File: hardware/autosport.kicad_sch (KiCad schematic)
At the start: 11 parts

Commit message: Add the Cube project
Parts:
- removed J?: AS022-55SN, symbol Connector_Generic:Conn_2Rows-55Pins
- removed R26, R27, R28: 0R, symbol Device:R_Small
- added J2: AS022-55SN, Local_Library:AS022-55SN, symbol AS022-55SN:AS022-55SN
- added R21, R22, R23, R24: 0R, symbol Device:R_Small
- renumbered R21 to R25, R22 to R26, R23 to R27, R24 to R28, R25 to R29, R29 to R30, R30 to R31
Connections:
- net +24V: now also J2.1 (Pin_1), J2.2 (Pin_2), J2.29 (Pin_29)
- net 5V_AUX: now also J2.54 (Pin_54)
- net ANALOG_INPUT_IN1: now also R21.1
- net ANALOG_INPUT_IN2: now also R22.1
- net ANALOG_INPUT_IN3: now also R23.1
- net ANALOG_INPUT_IN4: now also R24.1
- net ASSI_OUT_B: now also J2.37 (Pin_37)
- net ASSI_OUT_G: now also J2.36 (Pin_36)
- net ASSI_OUT_R: now also J2.35 (Pin_35)
- net BRAKE_LIGHT_OUT: now also J2.30 (Pin_30)
- net CAN+: now also J2.3 (Pin_3)
- net CAN-: now also J2.4 (Pin_4)
- net CAN2+: now also J2.5 (Pin_5)
- net CAN2-: now also J2.6 (Pin_6)
- net FAN_OUT_L: now also J2.31 (Pin_31)
- net FAN_OUT_R: now also J2.32 (Pin_32)
- net GND: now also J2.27 (Pin_27), J2.28 (Pin_28), J2.55 (Pin_55)
- net MONO_TEMPERATURE_IN: now also J2.11 (Pin_11)
- net PUMP_OUT_L: now also J2.33 (Pin_33)
- net PUMP_OUT_R: now also J2.34 (Pin_34)
- net RTDS_OUT: now also J2.51 (Pin_51)
- net SAFETY_IN_ASMS: now also J2.44 (Pin_44)
- net SAFETY_IN_FW: now also J2.43 (Pin_43)
- net SAFETY_IN_HV: now also J2.42 (Pin_42)
- net SAFETY_IN_HVD: now also J2.40 (Pin_40)
- net SAFETY_IN_INV: now also J2.39 (Pin_39)
- net SAFETY_IN_RES: now also J2.41 (Pin_41)
- net SAFETY_IN_RFU1: now also J2.45 (Pin_45)
- net SAFETY_IN_RFU2: now also J2.46 (Pin_46)
- net WATER_PRESSURE_IN1: now also J2.7 (Pin_7)
- net WATER_PRESSURE_IN2: now also J2.8 (Pin_8)
- net WATER_TEMPERATURE_IN1: now also J2.9 (Pin_9)
- net WATER_TEMPERATURE_IN2: now also J2.10 (Pin_10)
- net at R26.2: now also J2.21 (Pin_21)
- net at R29.2: now also J2.24 (Pin_24)
- net at R27.2: now also J2.22 (Pin_22)
- net at R25.2: now also J2.20 (Pin_20)
- net at R28.2: now also J2.23 (Pin_23)
- net at R30.2: now also J2.25 (Pin_25)
- net at R31.2: now also J2.26 (Pin_26)
- new net: J2.14 (Pin_14), R21.2
- new net: J2.15 (Pin_15), R22.2
- new net: J2.16 (Pin_16), R23.2
- new net: J2.17 (Pin_17), R24.2
- new net ASSI_OUT_BUZZER: J2.38 (Pin_38)
- new net SAFETY_IN_WHEEL_FL: J2.47 (Pin_47)
- new net SAFETY_IN_WHEEL_FR: J2.48 (Pin_48)
- new net SAFETY_IN_WHEEL_RL: J2.49 (Pin_49)
- new net SAFETY_IN_WHEEL_RR: J2.50 (Pin_50)
- new net SUSPENSION_POT_IN_L: J2.12 (Pin_12)
- new net SUSPENSION_POT_IN_R: J2.13 (Pin_13)
- no-connect marks 3 -> 4
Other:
- note removed: "Additional interfaces"
- note removed: "RFU: Shielding?"
- moved on the sheet: R25, R26, R27, R28, R29, R30, R31

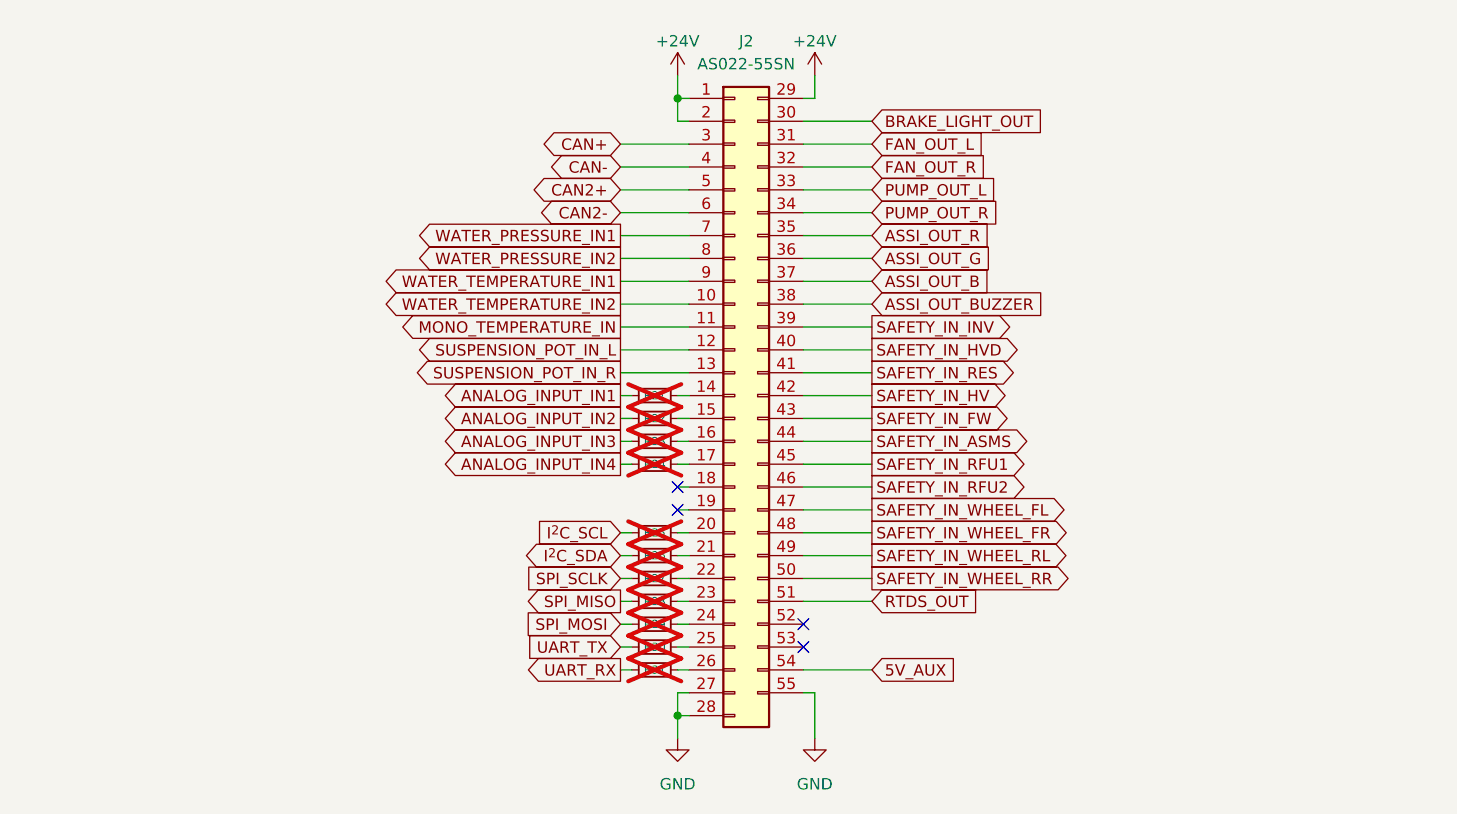
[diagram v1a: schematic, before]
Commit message: Improve the schematic
- add anti-aliasing filters
- rearrange the main connector signals
- improve the power filtering
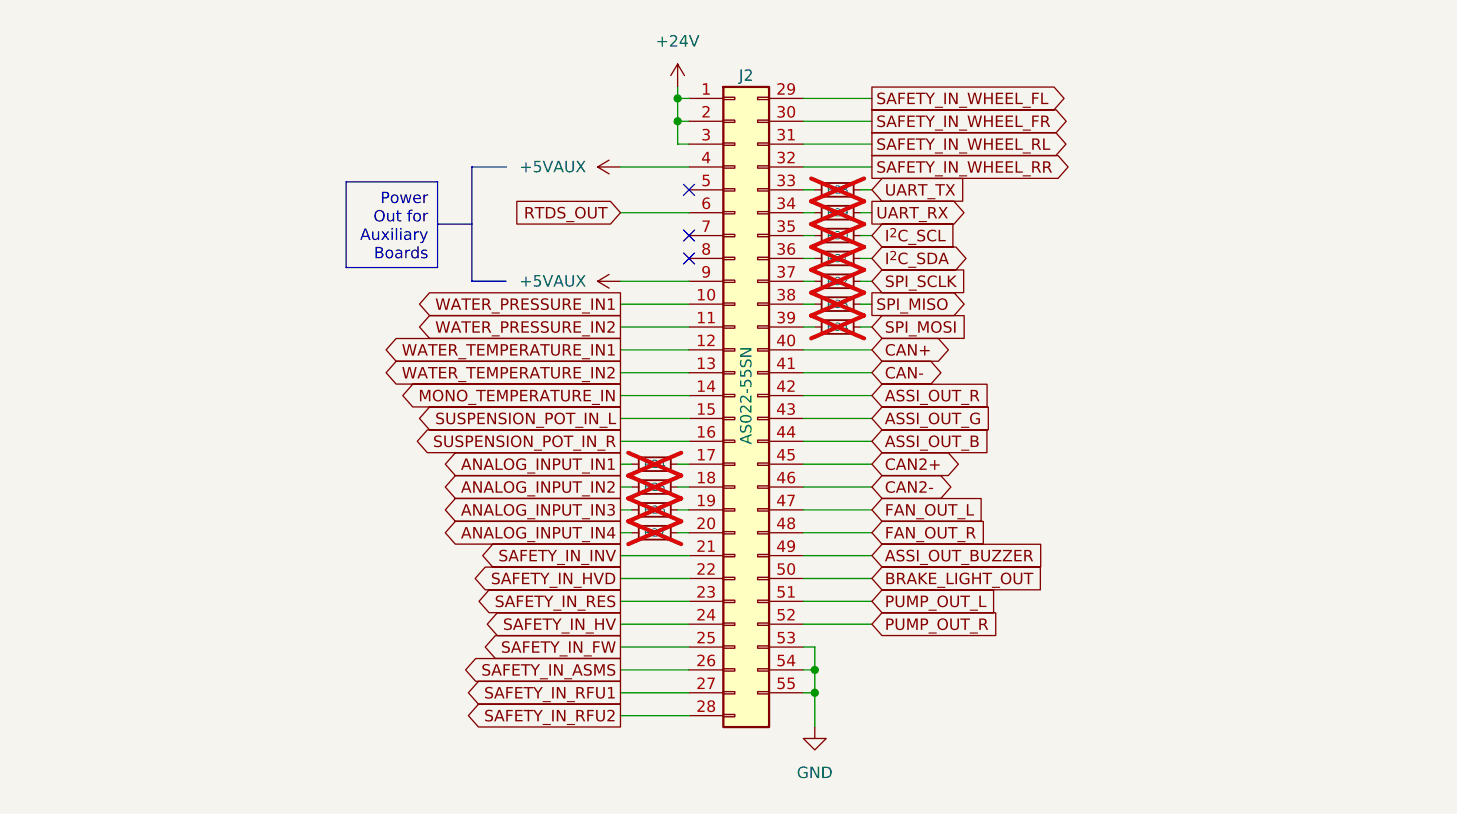
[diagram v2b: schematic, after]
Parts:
- R24: renamed from R21; footprint (none) -> Resistor_SMD:R_0603_1608Metric
- R25: renamed from R22; footprint (none) -> Resistor_SMD:R_0603_1608Metric
- R26: renamed from R23; footprint (none) -> Resistor_SMD:R_0603_1608Metric
- R27: renamed from R24; footprint (none) -> Resistor_SMD:R_0603_1608Metric
- R28: renamed from R25; footprint (none) -> Resistor_SMD:R_0603_1608Metric
- R29: renamed from R26; footprint (none) -> Resistor_SMD:R_0603_1608Metric
- R30: renamed from R27; footprint (none) -> Resistor_SMD:R_0603_1608Metric
- R31: renamed from R28; footprint (none) -> Resistor_SMD:R_0603_1608Metric
- R32: renamed from R29; footprint (none) -> Resistor_SMD:R_0603_1608Metric
- R33: renamed from R30; footprint (none) -> Resistor_SMD:R_0603_1608Metric
- R34: renamed from R31; footprint (none) -> Resistor_SMD:R_0603_1608Metric
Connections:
- net 5V_AUX is gone; now on net GND: J2.54 (Pin_54)
- net +24V: now also J2.3 (Pin_3); no longer J2.29 (Pin_29)
- net ASSI_OUT_B: now also J2.44 (Pin_44); no longer J2.37 (Pin_37)
- net ASSI_OUT_BUZZER: now also J2.49 (Pin_49); no longer J2.38 (Pin_38)
- net ASSI_OUT_G: now also J2.43 (Pin_43); no longer J2.36 (Pin_36)
- net ASSI_OUT_R: now also J2.42 (Pin_42); no longer J2.35 (Pin_35)
- net BRAKE_LIGHT_OUT: now also J2.50 (Pin_50); no longer J2.30 (Pin_30)
- net CAN+: now also J2.40 (Pin_40); no longer J2.3 (Pin_3)
- net CAN-: now also J2.41 (Pin_41); no longer J2.4 (Pin_4)
- net CAN2+: now also J2.45 (Pin_45); no longer J2.5 (Pin_5)
- net CAN2-: now also J2.46 (Pin_46); no longer J2.6 (Pin_6)
- net FAN_OUT_L: now also J2.47 (Pin_47); no longer J2.31 (Pin_31)
- net FAN_OUT_R: now also J2.48 (Pin_48); no longer J2.32 (Pin_32)
- net GND: now also J2.53 (Pin_53); no longer J2.27 (Pin_27), J2.28 (Pin_28)
- net I^{2}C_SCL: now also R30.2; no longer R28.1
- net I^{2}C_SDA: now also R31.2; no longer R29.1
- net MONO_TEMPERATURE_IN: now also J2.14 (Pin_14); no longer J2.11 (Pin_11)
- net PUMP_OUT_L: now also J2.51 (Pin_51); no longer J2.33 (Pin_33)
- net PUMP_OUT_R: now also J2.52 (Pin_52); no longer J2.34 (Pin_34)
- net RTDS_OUT: now also J2.6 (Pin_6); no longer J2.51 (Pin_51)
- net SAFETY_IN_ASMS: now also J2.26 (Pin_26); no longer J2.44 (Pin_44)
- net SAFETY_IN_FW: now also J2.25 (Pin_25); no longer J2.43 (Pin_43)
- net SAFETY_IN_HV: now also J2.24 (Pin_24); no longer J2.42 (Pin_42)
- net SAFETY_IN_HVD: now also J2.22 (Pin_22); no longer J2.40 (Pin_40)
- net SAFETY_IN_INV: now also J2.21 (Pin_21); no longer J2.39 (Pin_39)
- net SAFETY_IN_RES: now also J2.23 (Pin_23); no longer J2.41 (Pin_41)
- net SAFETY_IN_RFU1: now also J2.27 (Pin_27); no longer J2.45 (Pin_45)
- net SAFETY_IN_RFU2: now also J2.28 (Pin_28); no longer J2.46 (Pin_46)
- net SAFETY_IN_WHEEL_FL: now also J2.29 (Pin_29); no longer J2.47 (Pin_47)
- net SAFETY_IN_WHEEL_FR: now also J2.30 (Pin_30); no longer J2.48 (Pin_48)
- net SAFETY_IN_WHEEL_RL: now also J2.31 (Pin_31); no longer J2.49 (Pin_49)
- net SAFETY_IN_WHEEL_RR: now also J2.32 (Pin_32); no longer J2.50 (Pin_50)
- net SPI_MISO: now also R33.2; no longer R31.1
- net SPI_MOSI: now also R34.2; no longer R32.1
- net SPI_SCLK: now also R32.2; no longer R30.1
- net SUSPENSION_POT_IN_L: now also J2.15 (Pin_15); no longer J2.12 (Pin_12)
- net SUSPENSION_POT_IN_R: now also J2.16 (Pin_16); no longer J2.13 (Pin_13)
- net UART_RX: now also R29.2; no longer R34.1
- net UART_TX: now also R28.2; no longer R33.1
- net WATER_PRESSURE_IN1: now also J2.10 (Pin_10); no longer J2.7 (Pin_7)
- net WATER_PRESSURE_IN2: now also J2.11 (Pin_11); no longer J2.8 (Pin_8)
- net WATER_TEMPERATURE_IN1: now also J2.12 (Pin_12); no longer J2.9 (Pin_9)
- net WATER_TEMPERATURE_IN2: now also J2.13 (Pin_13); no longer J2.10 (Pin_10)
- net at R24.2: now also J2.17 (Pin_17); no longer J2.14 (Pin_14)
- net at R25.2: now also J2.18 (Pin_18); no longer J2.15 (Pin_15)
- net at R26.2: now also J2.19 (Pin_19); no longer J2.16 (Pin_16)
- net at R27.2: now also J2.20 (Pin_20); no longer J2.17 (Pin_17)
- new net: J2.34 (Pin_34), R29.1
- new net: J2.33 (Pin_33), R28.1
- new net: J2.35 (Pin_35), R30.1
- new net: J2.36 (Pin_36), R31.1
- new net: J2.37 (Pin_37), R32.1
- new net: J2.38 (Pin_38), R33.1
- new net: J2.39 (Pin_39), R34.1
- new net +5VAUX: J2.4 (Pin_4), J2.9 (Pin_9)
- no-connect marks 4 -> 3
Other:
- moved on the sheet: R24, R25, R26, R27, R28, R29, R30, R31, R32, R33, R34

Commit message: Set component values
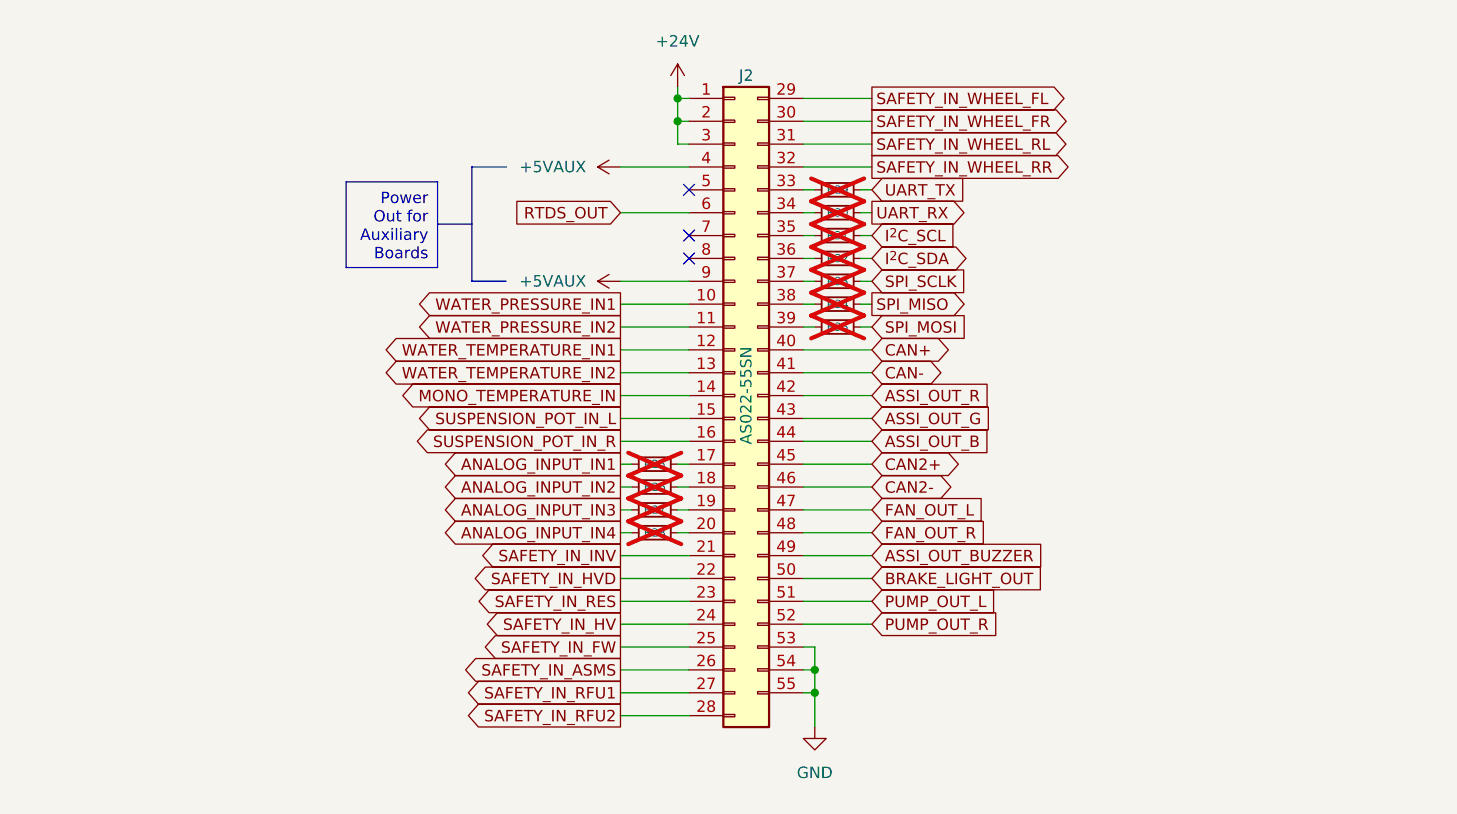
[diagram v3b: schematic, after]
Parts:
- renumbered R24 to R25, R25 to R26, R26 to R27, R27 to R28, R28 to R29, R29 to R30, R30 to R31, R31 to R32, R32 to R33, R33 to R34, R34 to R35
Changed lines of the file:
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@@
   (symbol (lib_id "Device:R_Small") (at 160.02 80.01 90) (unit 1)
     (in_bom yes) (on_board yes) (dnp yes)
-    (property "Reference" "R29" (at 160.02 80.01 90)
+    (property "Reference" "R30" (at 160.02 80.01 90)
       (effects (font (size 0.9 0.9)))
     )
@@
       (project "rearbox"
         (path "/b652b05a-4e3d-4ad1-b032-18886abe7d45/cf65c657-8245-46fb-8929-d241bd579513"
-          (reference "R29") (unit 1)
+          (reference "R30") (unit 1)
         )
       )
@@
   (symbol (lib_id "Device:R_Small") (at 160.02 87.63 90) (unit 1)
     (in_bom yes) (on_board yes) (dnp yes)
-    (property "Reference" "R32" (at 160.02 87.63 90)
+    (property "Reference" "R33" (at 160.02 87.63 90)
       (effects (font (size 0.9 0.9)))
     )
@@
       (project "rearbox"
         (path "/b652b05a-4e3d-4ad1-b032-18886abe7d45/cf65c657-8245-46fb-8929-d241bd579513"
-          (reference "R32") (unit 1)
+          (reference "R33") (unit 1)
         )
       )
@@
   (symbol (lib_id "Device:R_Small") (at 160.02 82.55 90) (unit 1)
     (in_bom yes) (on_board yes) (dnp yes)
-    (property "Reference" "R30" (at 160.02 82.55 90)
+    (property "Reference" "R31" (at 160.02 82.55 90)
       (effects (font (size 0.9 0.9)))
     )
@@
       (project "rearbox"
         (path "/b652b05a-4e3d-4ad1-b032-18886abe7d45/cf65c657-8245-46fb-8929-d241bd579513"
-          (reference "R30") (unit 1)
+          (reference "R31") (unit 1)
         )
       )
@@
   (symbol (lib_id "Device:R_Small") (at 160.02 77.47 90) (unit 1)
     (in_bom yes) (on_board yes) (dnp yes)
-    (property "Reference" "R28" (at 160.02 77.47 90)
+    (property "Reference" "R29" (at 160.02 77.47 90)
       (effects (font (size 0.9 0.9)))
     )
@@
       (project "rearbox"
         (path "/b652b05a-4e3d-4ad1-b032-18886abe7d45/cf65c657-8245-46fb-8929-d241bd579513"
+          (reference "R29") (unit 1)
+        )
+      )
+    )
+  )
+  (symbol (lib_id "Device:R_Small") (at 139.7 115.57 90) (unit 1)
+    (in_bom yes) (on_board yes) (dnp yes)
+    (property "Reference" "R28" (at 139.7 115.57 90)
+      (effects (font (size 0.9 0.9)))
+    )
+    (property "Value" "0R" (at 139.7 118.11 90)
+      (effects (font (size 1.27 1.27)) hide)
+    )
+    (property "Footprint" "Resistor_SMD:R_0603_1608Metric" (at 139.7 115.57 0)
+      (effects (font (size 1.27 1.27)) hide)
+    )
+    (property "Datasheet" "~" (at 139.7 115.57 0)
+      (effects (font (size 1.27 1.27)) hide)
+    )
+    (pin "1")
+    (pin "2")
+    (instances
+      (project "rearbox"
+        (path "/b652b05a-4e3d-4ad1-b032-18886abe7d45/cf65c657-8245-46fb-8929-d241bd579513"
           (reference "R28") (unit 1)
-        )
-      )
-    )
-  )
-  (symbol (lib_id "Device:R_Small") (at 139.7 115.57 90) (unit 1)
-    (in_bom yes) (on_board yes) (dnp yes)
-    (property "Reference" "R27" (at 139.7 115.57 90)
-      (effects (font (size 0.9 0.9)))
-    )
-    (property "Value" "0R" (at 139.7 118.11 90)
-      (effects (font (size 1.27 1.27)) hide)
-    )
-    (property "Footprint" "Resistor_SMD:R_0603_1608Metric" (at 139.7 115.57 0)
-      (effects (font (size 1.27 1.27)) hide)
-    )
-    (property "Datasheet" "~" (at 139.7 115.57 0)
-      (effects (font (size 1.27 1.27)) hide)
-    )
-    (pin "1")
-    (pin "2")
-    (instances
-      (project "rearbox"
-        (path "/b652b05a-4e3d-4ad1-b032-18886abe7d45/cf65c657-8245-46fb-8929-d241bd579513"
-          (reference "R27") (unit 1)
         )
       )
@@
   (symbol (lib_id "Device:R_Small") (at 160.02 85.09 90) (unit 1)
     (in_bom yes) (on_board yes) (dnp yes)
-    (property "Reference" "R31" (at 160.02 85.09 90)
+    (property "Reference" "R32" (at 160.02 85.09 90)
       (effects (font (size 0.9 0.9)))
     )
@@
       (project "rearbox"
         (path "/b652b05a-4e3d-4ad1-b032-18886abe7d45/cf65c657-8245-46fb-8929-d241bd579513"
-          (reference "R31") (unit 1)
+          (reference "R32") (unit 1)
         )
       )
@@
   (symbol (lib_id "Device:R_Small") (at 139.7 110.49 90) (unit 1)
     (in_bom yes) (on_board yes) (dnp yes)
-    (property "Reference" "R25" (at 139.7 110.49 90)
+    (property "Reference" "R26" (at 139.7 110.49 90)
       (effects (font (size 0.9 0.9)))
     )
@@
       (project "rearbox"
         (path "/b652b05a-4e3d-4ad1-b032-18886abe7d45/cf65c657-8245-46fb-8929-d241bd579513"
-          (reference "R25") (unit 1)
+          (reference "R26") (unit 1)
         )
       )
@@
   (symbol (lib_id "Device:R_Small") (at 139.7 107.95 90) (unit 1)
     (in_bom yes) (on_board yes) (dnp yes)
-    (property "Reference" "R24" (at 139.7 107.95 90)
+    (property "Reference" "R25" (at 139.7 107.95 90)
       (effects (font (size 0.9 0.9)))
     )
@@
       (project "rearbox"
         (path "/b652b05a-4e3d-4ad1-b032-18886abe7d45/cf65c657-8245-46fb-8929-d241bd579513"
-          (reference "R24") (unit 1)
+          (reference "R25") (unit 1)
         )
       )
@@
   (symbol (lib_id "Device:R_Small") (at 160.02 90.17 90) (unit 1)
     (in_bom yes) (on_board yes) (dnp yes)
-    (property "Reference" "R33" (at 160.02 90.17 90)
+    (property "Reference" "R34" (at 160.02 90.17 90)
       (effects (font (size 0.9 0.9)))
     )
@@
       (project "rearbox"
         (path "/b652b05a-4e3d-4ad1-b032-18886abe7d45/cf65c657-8245-46fb-8929-d241bd579513"
-          (reference "R33") (unit 1)
+          (reference "R34") (unit 1)
         )
       )
@@
   (symbol (lib_id "Device:R_Small") (at 139.7 113.03 90) (unit 1)
     (in_bom yes) (on_board yes) (dnp yes)
-    (property "Reference" "R26" (at 139.7 113.03 90)
+    (property "Reference" "R27" (at 139.7 113.03 90)
       (effects (font (size 0.9 0.9)))
     )
@@
       (project "rearbox"
         (path "/b652b05a-4e3d-4ad1-b032-18886abe7d45/cf65c657-8245-46fb-8929-d241bd579513"
-          (reference "R26") (unit 1)
+          (reference "R27") (unit 1)
         )
       )
@@
   (symbol (lib_id "Device:R_Small") (at 160.02 92.71 90) (unit 1)
     (in_bom yes) (on_board yes) (dnp yes)
-    (property "Reference" "R34" (at 160.02 92.71 90)
+    (property "Reference" "R35" (at 160.02 92.71 90)
       (effects (font (size 0.9 0.9)))
     )
@@
       (project "rearbox"
         (path "/b652b05a-4e3d-4ad1-b032-18886abe7d45/cf65c657-8245-46fb-8929-d241bd579513"
-          (reference "R34") (unit 1)
-        )
-      )
+          (reference "R35") (unit 1)
+        )
+      )
